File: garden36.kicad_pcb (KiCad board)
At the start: 2 copper layers, 41 parts, among them J1 Conn_01x02, SW1 SW_SPDT, SW2 SW_Push, U1 nice_nano

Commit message: Move PCB board around
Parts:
- CH1, CH10, CH11, CH12, CH13, CH14, CH15, CH16, CH17, CH18, CH2, CH3, CH4, CH5, CH6, CH7, CH8, CH9, D1, D10, D11, D12, D13, D14, D15, D16, D17, D18, D2, D3, D4, D5, D6, D7, D8, D9: moved to B.Cu
- moved D11 133.5 mm to (37.1, 86.1), turned to 90 degrees
- moved D1 131.9 mm to (37.1, 51.9), turned to 90 degrees
- moved D6 131.7 mm to (37.1, 69.1), turned to 90 degrees
- moved D12 115.9 mm to (55.1, 86.1), turned to 90 degrees
- moved D2 115.5 mm to (55.1, 52.1), turned to 90 degrees
- moved D7 115.5 mm to (55.1, 69.1), turned to 90 degrees
- moved CH6 101.0 mm to (30.4, 62.5), turned to 180 degrees
- moved D3 100.0 mm to (73.1, 52.1), turned to 90 degrees
- moved D8 98.6 mm to (73.1, 69.1), turned to 90 degrees
- moved D13 98.6 mm to (73.1, 86.1), turned to 90 degrees
- moved CH11 96.5 mm to (30.4, 79.5), turned to 180 degrees
- moved CH12 89.4 mm to (48.4, 79.5), turned to 180 degrees
- moved D4 85.5 mm to (91.1, 52.1), turned to 90 degrees
- moved D16 83.1 mm to (94.5, 105.0), turned to 90 degrees
- moved D9 81.7 mm to (91.1, 69.1), turned to 90 degrees
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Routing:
- net ROW2: track 0.00 -> 72.0 mm
- net ROW1: track 0.00 -> 72.0 mm
- net Net-(D1-A): track 0.00 -> 2.62 mm
- net Net-(D5-A): track 0.00 -> 1.70 mm

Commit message: Finished basic layout without any routing
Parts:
- SW1: footprint Button_Switch_SMD:SW_SPDT_CK_JS102011SAQN -> PCM_marbastlib-various:SW_MSK12C02-HB
- SW2: footprint Button_Switch_SMD:SW_Tactile_SPST_NO_Straight_CK_PTS636Sx25SMTRLFS -> Button_Switch_SMD:SW_SPST_TL3305A
- U1: footprint PCM_marbastlib-xp-promicroish:nice_nano_AH_USBup -> PCM_marbastlib-xp-promicroish:nice_nano_AH_USBdn
- moved CH11 34.9 mm to (40.5, 112.9)
- moved CH1 34.9 mm to (40.5, 78.9)
- moved CH6 34.9 mm to (40.5, 95.9)
- moved CH17 31.5 mm to (117.1, 128.4), turned to 165 degrees
- moved CH16 29.3 mm to (96.9, 126.5)
- moved CH15 28.6 mm to (112.5, 106.2)
- moved CH10 28.6 mm to (112.5, 89.2)
- moved CH5 28.6 mm to (112.5, 72.2)
- moved D10 28.0 mm to (119.2, 95.2)
- moved D15 28.0 mm to (119.2, 112.2)
- moved D5 28.0 mm to (119.2, 78.2)
- moved CH12 22.8 mm to (58.5, 99.9)
- moved CH2 22.8 mm to (58.5, 65.9)
- moved CH7 22.8 mm to (58.5, 82.9)
- moved D1 22.6 mm to (40.5, 74.2), turned to 0 degrees
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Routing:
- net ROW2: track 72.0 -> 0.00 mm
- net ROW1: track 72.0 -> 0.00 mm
- net Net-(D1-A): track 2.62 -> 0.00 mm
- net Net-(D5-A): track 1.70 -> 0.00 mm
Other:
- board outline added: 113.4 x 90 mm
- rule pad_to_mask_clearance: 0 -> 0.038

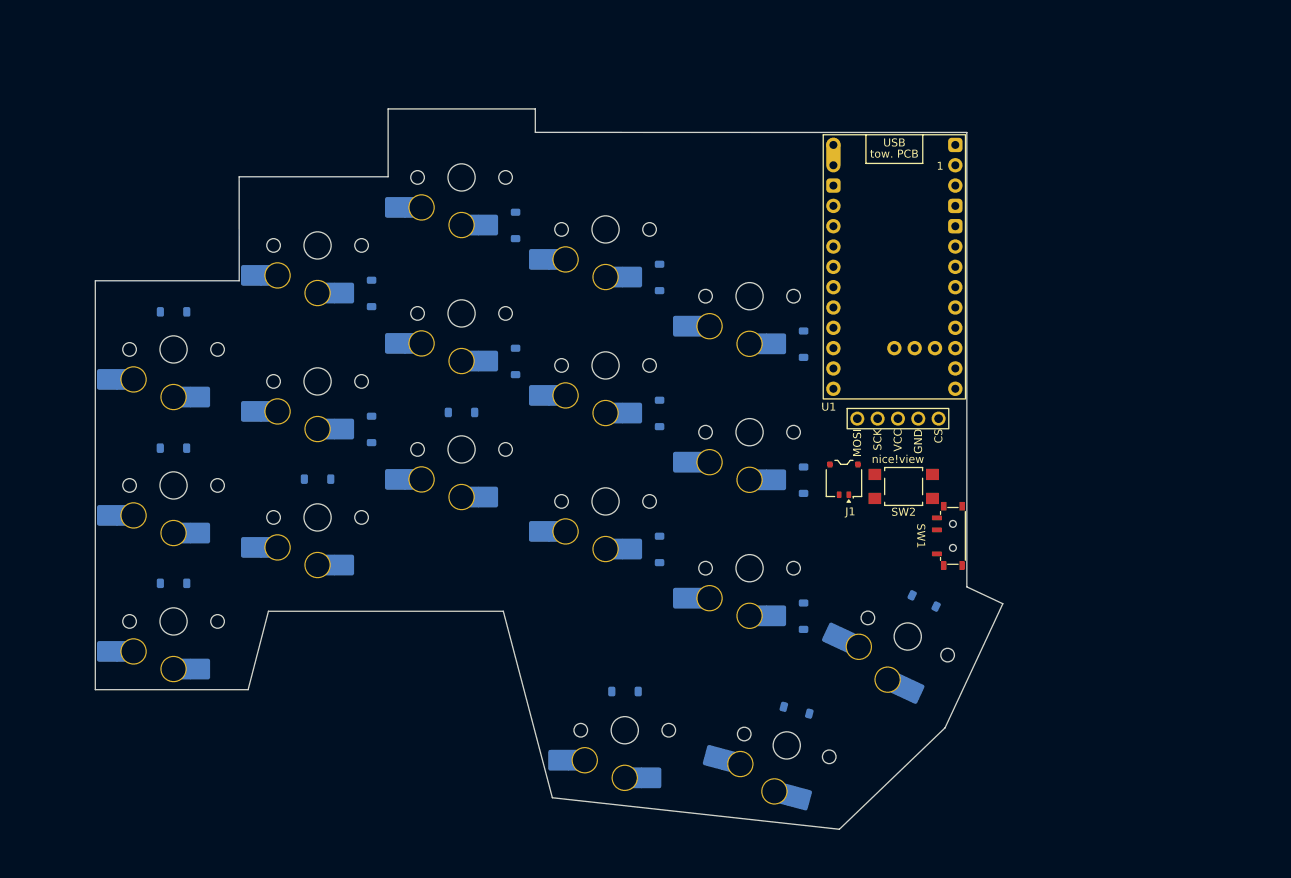
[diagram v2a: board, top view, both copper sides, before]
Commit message: Add v1.1 of buttons and update outline to 0.5mm
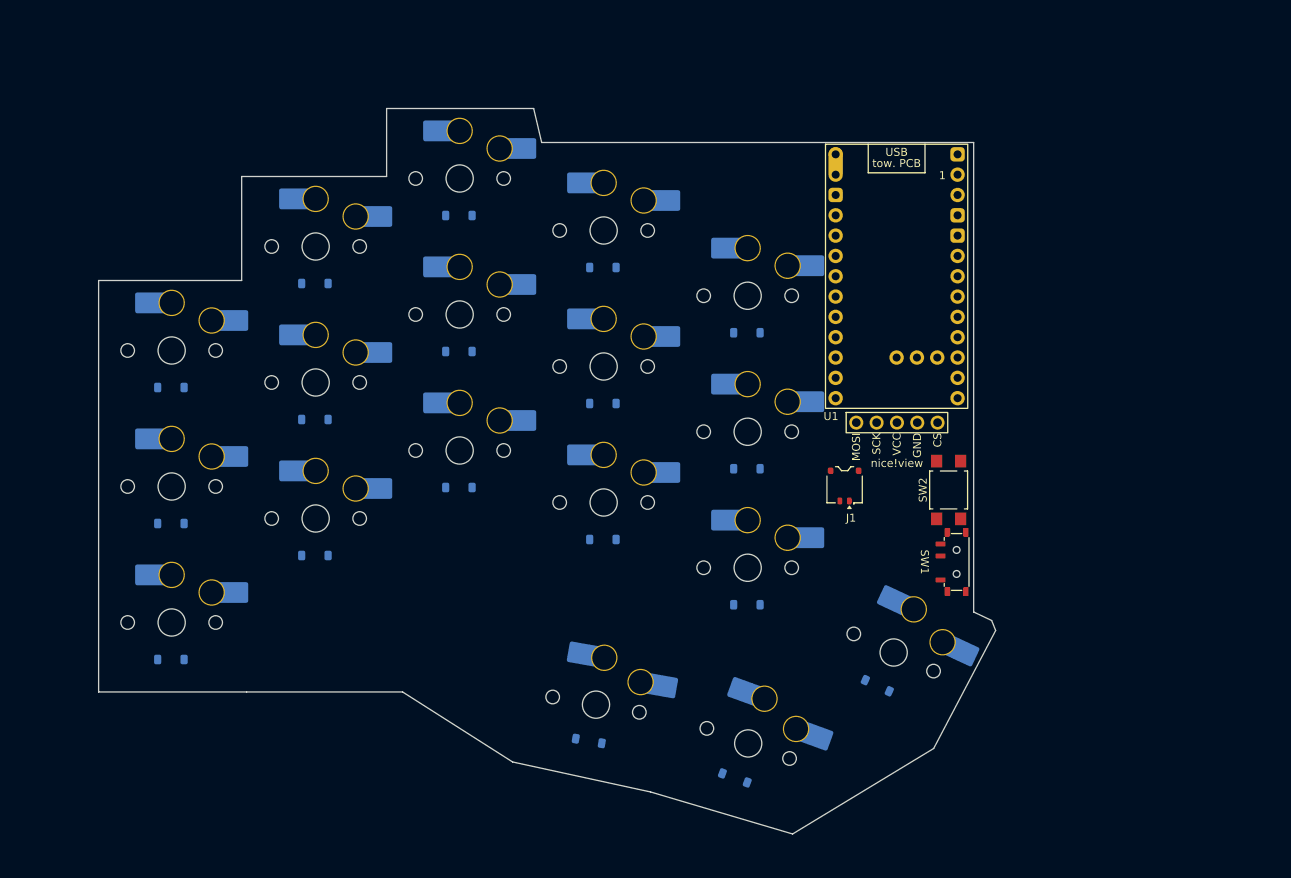
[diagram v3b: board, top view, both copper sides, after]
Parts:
- moved D18 12.1 mm to (128.5, 120.9), turned to 155 degrees
- moved D17 11.5 mm to (110.7, 132.4), turned to 160 degrees
- moved D12 9.56 mm to (58.2, 104.6), turned to 180 degrees
- moved D11 9.53 mm to (40.2, 117.6), turned to 180 degrees
- moved D1 9.46 mm to (40.2, 83.6), turned to 180 degrees
- moved D6 9.43 mm to (40.2, 100.6), turned to 180 degrees
- moved D13 9.39 mm to (76.2, 96.1), turned to 180 degrees
- moved D16 7.66 mm to (92.4, 127.8), turned to 170 degrees
- moved D10 7.23 mm to (112.2, 93.8), turned to 180 degrees
- moved D15 7.23 mm to (112.2, 110.8), turned to 180 degrees
- moved D5 7.23 mm to (112.2, 76.8), turned to 180 degrees
- moved D14 7.19 mm to (94.2, 102.6), turned to 180 degrees
- moved D2 7.19 mm to (58.2, 70.6), turned to 180 degrees
- moved D3 7.19 mm to (76.2, 62.1), turned to 180 degrees
- moved D4 7.19 mm to (94.2, 68.6), turned to 180 degrees
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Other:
- board size 113.4 x 90 mm -> 112.1 x 90.7 mm
